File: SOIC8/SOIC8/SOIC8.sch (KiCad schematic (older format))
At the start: 3 parts, among them J1 Conn_01x04, J2 Conn_01x04, U1 ATtiny85-20SU

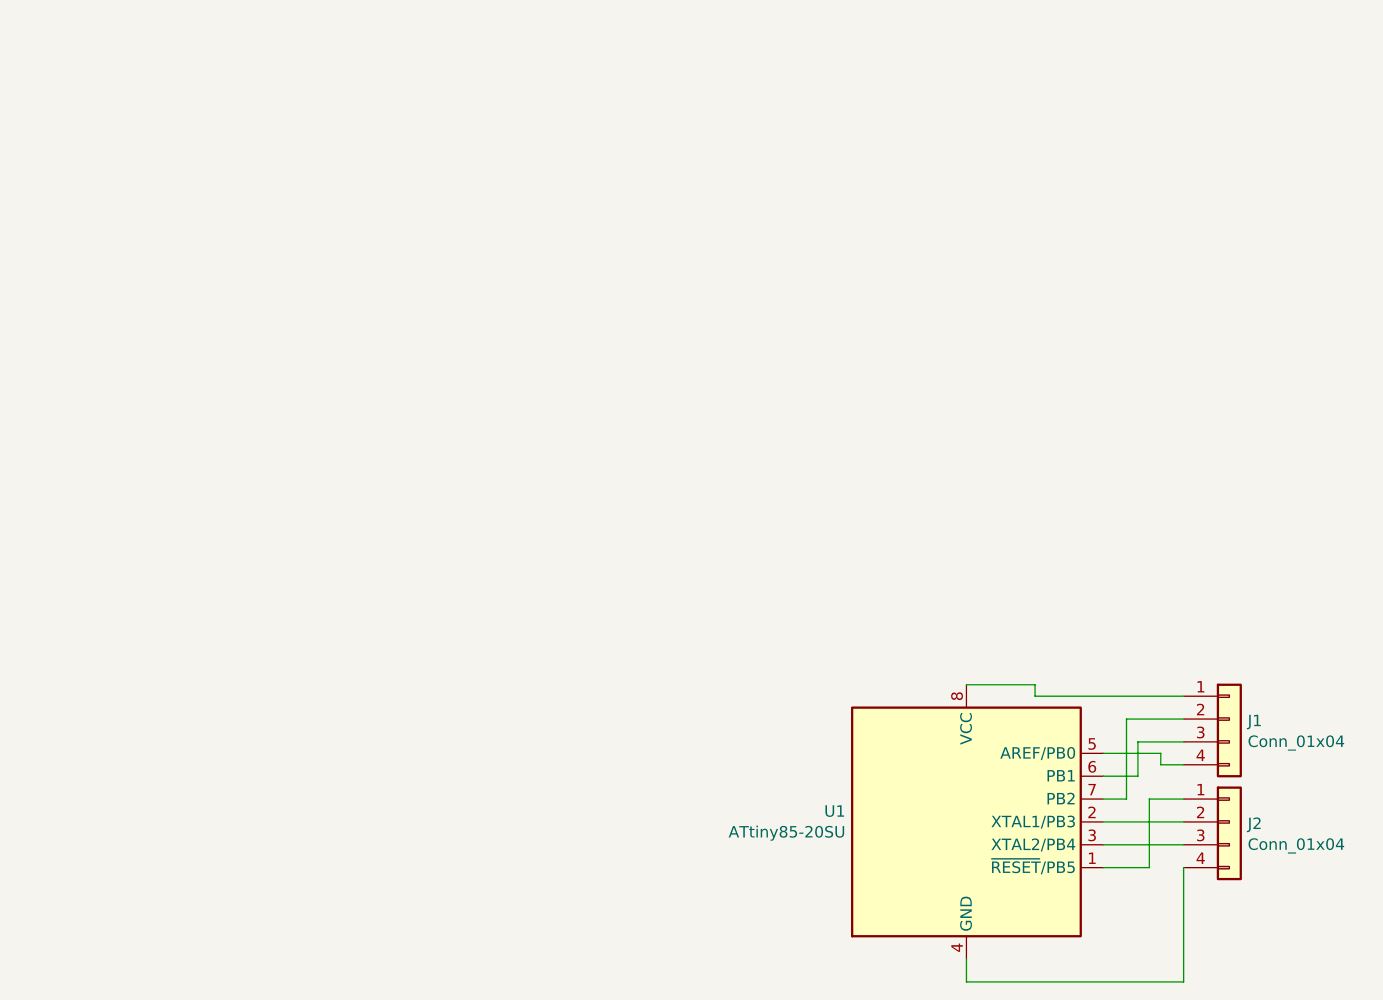
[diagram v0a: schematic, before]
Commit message: USB, SD and CR Cells Added
MicroSD, MicroUSB, MiniUSB, USB-C, CR1220, CR2032 added as well as all schematics page sizes optimised
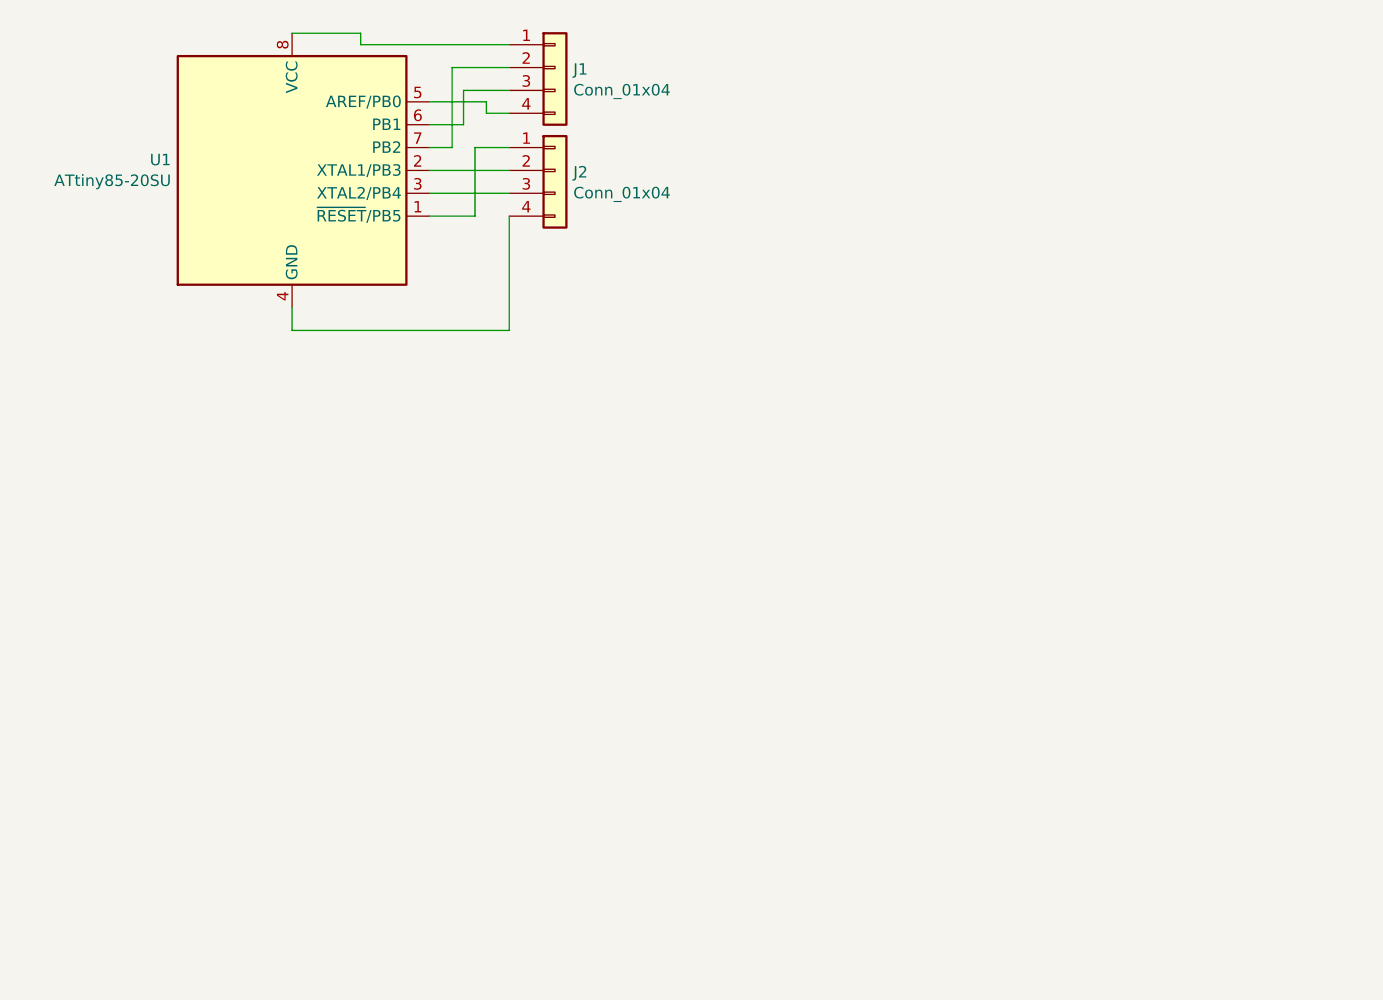
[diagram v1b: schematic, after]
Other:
- moved on the sheet: J1, J2, U1
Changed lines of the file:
@@
 EESchema Schematic File Version 4
+LIBS:SOIC8-cache
 EELAYER 29 0
 EELAYER END
-$Descr A4 11693 8268
+$Descr User 5197 4016
 encoding utf-8
 Sheet 1 1
-Title ""
-Date ""
-Rev ""
-Comp ""
-Comment1 ""
-Comment2 ""
-Comment3 ""
+Title "SOIC8 To DIP8 Breakout Board"
+Date "2019-07-04"
+Rev "1"
+Comp "SirBoard"
+Comment1 "SOIC8 P = 1.27mm"
+Comment2 "MSOP8 P = 0.65mm"
+Comment3 "DIP8 P = 2.54mm"
 Comment4 ""
 $EndDescr
@@
 L MCU_Microchip_ATtiny:ATtiny85-20SU U1
 U 1 1 5D1B7CEE
-P 5250 4200
-F 0 "U1" H 4721 4246 50  0000 R CNN
-F 1 "ATtiny85-20SU" H 4721 4155 50  0000 R CNN
-F 2 "Package_SO:SOIJ-8_5.3x5.3mm_P1.27mm" H 5250 4200 50  0001 C CIN
-F 3 "http://ww1.microchip.com/downloads/en/DeviceDoc/atmel-2586-avr-8-bit-microcontroller-attiny25-attiny45-attiny85_datasheet.pdf" H 5250 4200 50  0001 C CNN
-	1    5250 4200
+P 2300 1350
+F 0 "U1" H 1771 1396 50  0000 R CNN
+F 1 "ATtiny85-20SU" H 1771 1305 50  0000 R CNN
+F 2 "Package_SO:SOIJ-8_5.3x5.3mm_P1.27mm" H 2300 1350 50  0001 C CIN
+F 3 "http://ww1.microchip.com/downloads/en/DeviceDoc/atmel-2586-avr-8-bit-microcontroller-attiny25-attiny45-attiny85_datasheet.pdf" H 2300 1350 50  0001 C CNN
+	1    2300 1350
 	1    0    0    -1
 $EndComp
@@
 L Connector_Generic:Conn_01x04 J2
 U 1 1 5D1B8092
-P 6400 4200
-F 0 "J2" H 6480 4192 50  0000 L CNN
-F 1 "Conn_01x04" H 6480 4101 50  0000 L CNN
-F 2 "Connector_PinHeader_2.54mm:PinHeader_1x04_P2.54mm_Vertical" H 6400 4200 50  0001 C CNN
-F 3 "~" H 6400 4200 50  0001 C CNN
-	1    6400 4200
+P 3450 1350
+F 0 "J2" H 3530 1342 50  0000 L CNN
+F 1 "Conn_01x04" H 3530 1251 50  0000 L CNN
+F 2 "Connector_PinHeader_2.54mm:PinHeader_1x04_P2.54mm_Vertical" H 3450 1350 50  0001 C CNN
+F 3 "~" H 3450 1350 50  0001 C CNN
+	1    3450 1350
 	1    0    0    -1
 $EndComp
@@
 L Connector_Generic:Conn_01x04 J1
 U 1 1 5D1B8353
-P 6400 3750
-F 0 "J1" H 6480 3742 50  0000 L CNN
-F 1 "Conn_01x04" H 6480 3651 50  0000 L CNN
-F 2 "Connector_PinHeader_2.54mm:PinHeader_1x04_P2.54mm_Vertical" H 6400 3750 50  0001 C CNN
-F 3 "~" H 6400 3750 50  0001 C CNN
-	1    6400 3750
+P 3450 900
+F 0 "J1" H 3530 892 50  0000 L CNN
+F 1 "Conn_01x04" H 3530 801 50  0000 L CNN
+F 2 "Connector_PinHeader_2.54mm:PinHeader_1x04_P2.54mm_Vertical" H 3450 900 50  0001 C CNN
+F 3 "~" H 3450 900 50  0001 C CNN
+	1    3450 900
 	1    0    0    -1
 $EndComp
 Wire Wire Line
-	6200 4100 6050 4100
+	3250 1250 3100 1250
 Wire Wire Line
-	6050 4100 6050 4400
+	3100 1250 3100 1550
 Wire Wire Line
-	6050 4400 5850 4400
+	3100 1550 2900 1550
 Wire Wire Line
-	5850 4200 6200 4200
+	2900 1350 3250 1350
 Wire Wire Line
-	6200 4300 5850 4300
+	3250 1450 2900 1450
 Wire Wire Line
-	6200 4400 6200 4900
+	3250 1550 3250 2050
 Wire Wire Line
-	6200 4900 5250 4900
+	3250 2050 2300 2050
 Wire Wire Line
-	5250 4900 5250 4800
+	2300 2050 2300 1950
 Wire Wire Line
-	6200 3650 5550 3650
+	3250 800  2600 800
 Wire Wire Line
-	5550 3650 5550 3600
+	2600 800  2600 750
 Wire Wire Line
-	5550 3600 5250 3600
+	2600 750  2300 750
 Wire Wire Line
-	6200 3750 5950 3750
+	3250 900  3000 900
 Wire Wire Line
-	5950 3750 5950 4100
+	3000 900  3000 1250
 Wire Wire Line
-	5950 4100 5850 4100
+	3000 1250 2900 1250
 Wire Wire Line
-	6200 3850 6000 3850
+	3250 1000 3050 1000
 Wire Wire Line
-	6000 3850 6000 4000
+	3050 1000 3050 1150
 Wire Wire Line
-	6000 4000 5850 4000
+	3050 1150 2900 1150
 Wire Wire Line
-	6200 3950 6100 3950
+	3250 1100 3150 1100
 Wire Wire Line
-	6100 3950 6100 3900
+	3150 1100 3150 1050
 Wire Wire Line
-	6100 3900 5850 3900
+	3150 1050 2900 1050
 $EndSCHEMATC

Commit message: Board Updates
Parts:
- removed U1: ATtiny85-20SU, Package_SO:SOIJ-8_5.3x5.3mm_P1.27mm, symbol MCU_Microchip_ATtiny:ATtiny85-20SU
- added J3: SOIC8, Package_SO:SOIC-8_3.9x4.9mm_P1.27mm, symbol Connector_Generic:Conn_02x04_Counter_Clockwise
- added J4: VSSOP8, Package_SO:VSSOP-8_2.3x2mm_P0.5mm, symbol Connector_Generic:Conn_02x04_Counter_Clockwise
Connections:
- net at J2.1 (Pin_1): now also J3.1 (Pin_1), J4.8 (Pin_8)
- net at J2.2 (Pin_2): now also J3.2 (Pin_2), J4.7 (Pin_7)
- net at J2.3 (Pin_3): now also J3.3 (Pin_3), J4.6 (Pin_6)
- net at J2.4 (Pin_4): now also J3.4 (Pin_4), J4.5 (Pin_5)
- net at J1.4 (Pin_4): now also J3.5 (Pin_5), J4.4 (Pin_4)
- net at J1.3 (Pin_3): now also J3.6 (Pin_6), J4.3 (Pin_3)
- net at J1.2 (Pin_2): now also J3.7 (Pin_7), J4.2 (Pin_2)
- net at J1.1 (Pin_1): now also J3.8 (Pin_8), J4.1 (Pin_1)
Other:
- moved on the sheet: J1, J2
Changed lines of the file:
@@
 Sheet 1 1
 Title "SOIC8 To DIP8 Breakout Board"
-Date "2019-07-04"
-Rev "1"
+Date "2020-02-13"
+Rev "2"
 Comp "SirBoard"
 Comment1 "SOIC8 P = 1.27mm"
-Comment2 "MSOP8 P = 0.65mm"
+Comment2 "VSSOP8 P = 0.5mm"
 Comment3 "DIP8 P = 2.54mm"
 Comment4 ""
 $EndDescr
 $Comp
-L MCU_Microchip_ATtiny:ATtiny85-20SU U1
-U 1 1 5D1B7CEE
-P 2300 1350
-F 0 "U1" H 1771 1396 50  0000 R CNN
-F 1 "ATtiny85-20SU" H 1771 1305 50  0000 R CNN
-F 2 "Package_SO:SOIJ-8_5.3x5.3mm_P1.27mm" H 2300 1350 50  0001 C CIN
-F 3 "http://ww1.microchip.com/downloads/en/DeviceDoc/atmel-2586-avr-8-bit-microcontroller-attiny25-attiny45-attiny85_datasheet.pdf" H 2300 1350 50  0001 C CNN
-	1    2300 1350
-	1    0    0    -1
-$EndComp
-$Comp
 L Connector_Generic:Conn_01x04 J2
 U 1 1 5D1B8092
-P 3450 1350
-F 0 "J2" H 3530 1342 50  0000 L CNN
-F 1 "Conn_01x04" H 3530 1251 50  0000 L CNN
-F 2 "Connector_PinHeader_2.54mm:PinHeader_1x04_P2.54mm_Vertical" H 3450 1350 50  0001 C CNN
-F 3 "~" H 3450 1350 50  0001 C CNN
-	1    3450 1350
-	1    0    0    -1
+P 1825 1700
+F 0 "J2" H 1905 1692 50  0000 L CNN
+F 1 "Conn_01x04" H 1905 1601 50  0001 L CNN
+F 2 "Connector_PinHeader_2.54mm:PinHeader_1x04_P2.54mm_Vertical" H 1825 1700 50  0001 C CNN
+F 3 "~" H 1825 1700 50  0001 C CNN
+	1    1825 1700
+	-1   0    0    -1
 $EndComp
 $Comp
 L Connector_Generic:Conn_01x04 J1
 U 1 1 5D1B8353
-P 3450 900
-F 0 "J1" H 3530 892 50  0000 L CNN
-F 1 "Conn_01x04" H 3530 801 50  0000 L CNN
-F 2 "Connector_PinHeader_2.54mm:PinHeader_1x04_P2.54mm_Vertical" H 3450 900 50  0001 C CNN
-F 3 "~" H 3450 900 50  0001 C CNN
-	1    3450 900
+P 3075 1700
+F 0 "J1" H 3155 1692 50  0000 L CNN
+F 1 "Conn_01x04" H 3155 1601 50  0001 L CNN
+F 2 "Connector_PinHeader_2.54mm:PinHeader_1x04_P2.54mm_Vertical" H 3075 1700 50  0001 C CNN
+F 3 "~" H 3075 1700 50  0001 C CNN
+	1    3075 1700
+	1    0    0    -1
+$EndComp
+$Comp
+L Connector_Generic:Conn_02x04_Counter_Clockwise J4
+U 1 1 5E452362
+P 2500 1050
+F 0 "J4" H 2550 1365 50  0000 C CNN
+F 1 "VSSOP8" H 2550 1275 50  0000 C CNN
+F 2 "Package_SO:VSSOP-8_2.3x2mm_P0.5mm" H 2500 1050 50  0001 C CNN
+F 3 "~" H 2500 1050 50  0001 C CNN
+	1    2500 1050
+	-1   0    0    -1
+$EndComp
+$Comp
+L Connector_Generic:Conn_02x04_Counter_Clockwise J3
+U 1 1 5E452B4C
+P 2400 1700
+F 0 "J3" H 2450 2015 50  0000 C CNN
+F 1 "SOIC8" H 2450 1925 50  0000 C CNN
+F 2 "Package_SO:SOIC-8_3.9x4.9mm_P1.27mm" H 2400 1700 50  0001 C CNN
+F 3 "~" H 2400 1700 50  0001 C CNN
+	1    2400 1700
 	1    0    0    -1
 $EndComp
 Wire Wire Line
-	3250 1250 3100 1250
+	2700 950  2875 950
 Wire Wire Line
-	3100 1250 3100 1550
+	2700 1050 2825 1050
 Wire Wire Line
-	3100 1550 2900 1550
+	2700 1150 2775 1150
 Wire Wire Line
-	2900 1350 3250 1350
+	2775 1150 2775 1800
 Wire Wire Line
-	3250 1450 2900 1450
+	2700 1250 2725 1250
 Wire Wire Line
-	3250 1550 3250 2050
+	2725 1250 2725 1900
 Wire Wire Line
-	3250 2050 2300 2050
+	2700 1700 2825 1700
 Wire Wire Line
-	2300 2050 2300 1950
+	2700 1800 2775 1800
 Wire Wire Line
-	3250 800  2600 800
+	2700 1900 2725 1900
+Connection ~ 2725 1900
+Connection ~ 2775 1800
+Connection ~ 2825 1700
 Wire Wire Line
-	2600 800  2600 750
+	2700 1600 2875 1600
 Wire Wire Line
-	2600 750  2300 750
+	2725 1900 2875 1900
 Wire Wire Line
-	3250 900  3000 900
+	2775 1800 2875 1800
 Wire Wire Line
-	3000 900  3000 1250
+	2825 1700 2875 1700
+Connection ~ 2875 1600
 Wire Wire Line
-	3000 1250 2900 1250
+	2825 1050 2825 1700
 Wire Wire Line
-	3250 1000 3050 1000
+	2875 950  2875 1600
 Wire Wire Line
-	3050 1000 3050 1150
+	2025 950  2025 1600
 Wire Wire Line
-	3050 1150 2900 1150
+	2075 1050 2075 1700
 Wire Wire Line
-	3250 1100 3150 1100
+	2175 1250 2175 1900
 Wire Wire Line
-	3150 1100 3150 1050
+	2200 1250 2175 1250
 Wire Wire Line
-	3150 1050 2900 1050
+	2125 1150 2125 1800
+Wire Wire Line
+	2200 1150 2125 1150
+Wire Wire Line
+	2200 1050 2075 1050
+Wire Wire Line
+	2200 950  2025 950
+Wire Wire Line
+	2200 1600 2025 1600
+Connection ~ 2025 1600
+Wire Wire Line
+	2025 1700 2075 1700
+Connection ~ 2075 1700
+Wire Wire Line
+	2075 1700 2200 1700
+Wire Wire Line
+	2200 1800 2125 1800
+Connection ~ 2125 1800
+Wire Wire Line
+	2125 1800 2025 1800
+Wire Wire Line
+	2025 1900 2175 1900
+Connection ~ 2175 1900
+Wire Wire Line
+	2175 1900 2200 1900
 $EndSCHEMATC
